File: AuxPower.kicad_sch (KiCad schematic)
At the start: 10 parts, among them J1 Conn_01x02_Female, U1 I6A4W020A033V-003-R

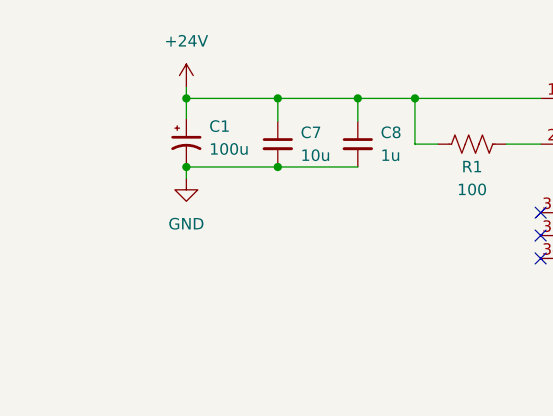
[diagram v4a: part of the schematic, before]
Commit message: Added 5V 9A buck converter
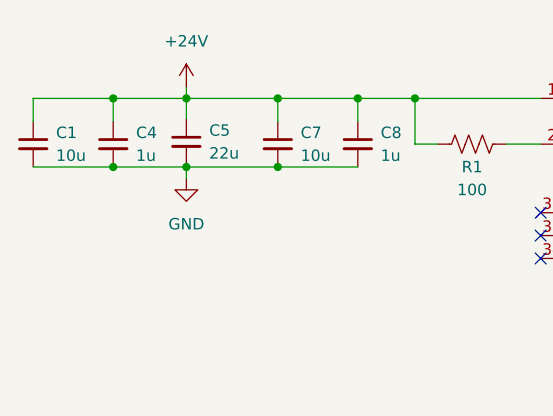
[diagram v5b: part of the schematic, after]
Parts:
- removed C1: 100u, Capacitor_SMD:CP_Elec_10x10, symbol Device:C_Polarized_Small_US
- added C1: 10u, Capacitor_SMD:C_0603_1608Metric, symbol Device:C_Small
- added C4: 1u, Capacitor_SMD:C_0603_1608Metric, symbol Device:C_Small
- added C5: 22u, Capacitor_Tantalum_SMD:CP_EIA-7343-15_Kemet-W, symbol Device:C_Small
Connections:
- net +24V: now also C1.1, C4.1, C5.1
- net GND: now also C1.2, C4.2, C5.2
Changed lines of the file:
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@@
 (kicad_sch (version 20211123) (generator eeschema)
   (paper "A4")
+  (junction (at 97.536 94.234) (diameter 0) (color 0 0 0 0)
+  )
+  (junction (at 79.248 94.234) (diameter 0) (color 0 0 0 0)
+  )
   (junction (at 157.226 86.614) (diameter 0) (color 0 0 0 0)
   )
@@
   (junction (at 171.196 94.234) (diameter 0) (color 0 0 0 0)
   )
-  (junction (at 97.536 94.234) (diameter 0) (color 0 0 0 0)
-  )
   (junction (at 87.376 86.614) (diameter 0) (color 0 0 0 0)
   )
   (junction (at 171.196 86.614) (diameter 0) (color 0 0 0 0)
   )
+  (junction (at 79.248 86.614) (diameter 0) (color 0 0 0 0)
+  )
   (junction (at 97.536 86.614) (diameter 0) (color 0 0 0 0)
   )
   (junction (at 149.606 112.014) (diameter 0) (color 0 0 0 0)
   )
+  (junction (at 87.376 94.234) (diameter 0) (color 0 0 0 0)
+  )
   (junction (at 141.986 112.014) (diameter 0) (color 0 0 0 0)
   )
@@
   )
   (junction (at 112.776 86.614) (diameter 0) (color 0 0 0 0)
-  )
-  (junction (at 87.376 94.234) (diameter 0) (color 0 0 0 0)
   )
   (junction (at 106.426 86.614) (diameter 0) (color 0 0 0 0)
@@
     (stroke (width 0) (type default) (color 0 0 0 0))
   )
+  (wire (pts (xy 70.358 94.234) (xy 79.248 94.234))
+    (stroke (width 0) (type default) (color 0 0 0 0))
+  )
   (wire (pts (xy 182.626 94.234) (xy 171.196 94.234))
     (stroke (width 0) (type default) (color 0 0 0 0))
@@
     (stroke (width 0) (type default) (color 0 0 0 0))
   )
-  (wire (pts (xy 87.376 94.234) (xy 97.536 94.234))
-    (stroke (width 0) (type default) (color 0 0 0 0))
-  )
   (wire (pts (xy 97.536 86.614) (xy 106.426 86.614))
     (stroke (width 0) (type default) (color 0 0 0 0))
@@
     (stroke (width 0) (type default) (color 0 0 0 0))
   )
+  (wire (pts (xy 70.358 86.614) (xy 79.248 86.614))
+    (stroke (width 0) (type default) (color 0 0 0 0))
+  )
   (wire (pts (xy 115.316 91.694) (xy 112.776 91.694))
     (stroke (width 0) (type default) (color 0 0 0 0))
   )
+  (wire (pts (xy 175.006 86.614) (xy 182.626 86.614))
+    (stroke (width 0) (type default) (color 0 0 0 0))
+  )
+  (wire (pts (xy 70.358 89.154) (xy 70.358 86.614))
+    (stroke (width 0) (type default) (color 0 0 0 0))
+  )
+  (wire (pts (xy 79.248 86.614) (xy 87.376 86.614))
+    (stroke (width 0) (type default) (color 0 0 0 0))
+  )
+  (wire (pts (xy 152.146 112.014) (xy 152.146 115.824))
+    (stroke (width 0) (type default) (color 0 0 0 0))
+  )
+  (wire (pts (xy 97.536 94.234) (xy 87.376 94.234))
+    (stroke (width 0) (type default) (color 0 0 0 0))
+  )
+  (wire (pts (xy 87.376 85.344) (xy 87.376 86.614))
+    (stroke (width 0) (type default) (color 0 0 0 0))
+  )
+  (wire (pts (xy 141.986 112.014) (xy 149.606 112.014))
+    (stroke (width 0) (type default) (color 0 0 0 0))
+  )
+  (wire (pts (xy 171.196 94.234) (xy 171.196 92.964))
+    (stroke (width 0) (type default) (color 0 0 0 0))
+  )
+  (wire (pts (xy 79.248 86.614) (xy 79.248 89.154))
+    (stroke (width 0) (type default) (color 0 0 0 0))
+  )
+  (wire (pts (xy 97.536 94.234) (xy 106.426 94.234))
+    (stroke (width 0) (type default) (color 0 0 0 0))
+  )
+  (wire (pts (xy 141.986 112.014) (xy 141.986 114.554))
+    (stroke (width 0) (type default) (color 0 0 0 0))
+  )
+  (wire (pts (xy 134.366 112.014) (xy 141.986 112.014))
+    (stroke (width 0) (type default) (color 0 0 0 0))
+  )
+  (wire (pts (xy 162.306 109.474) (xy 162.306 112.014))
+    (stroke (width 0) (type default) (color 0 0 0 0))
+  )
+  (wire (pts (xy 162.306 94.234) (xy 162.306 92.964))
+    (stroke (width 0) (type default) (color 0 0 0 0))
+  )
+  (wire (pts (xy 171.196 86.614) (xy 171.196 87.884))
+    (stroke (width 0) (type default) (color 0 0 0 0))
+  )
+  (wire (pts (xy 79.248 94.234) (xy 87.376 94.234))
+    (stroke (width 0) (type default) (color 0 0 0 0))
+  )
+  (wire (pts (xy 106.426 86.614) (xy 106.426 89.154))
+    (stroke (width 0) (type default) (color 0 0 0 0))
+  )
+  (wire (pts (xy 152.146 115.824) (xy 158.496 115.824))
+    (stroke (width 0) (type default) (color 0 0 0 0))
+  )
   (wire (pts (xy 87.376 94.234) (xy 87.376 95.504))
     (stroke (width 0) (type default) (color 0 0 0 0))
   )
-  (wire (pts (xy 175.006 86.614) (xy 182.626 86.614))
-    (stroke (width 0) (type default) (color 0 0 0 0))
-  )
-  (wire (pts (xy 152.146 112.014) (xy 152.146 115.824))
-    (stroke (width 0) (type default) (color 0 0 0 0))
-  )
-  (wire (pts (xy 87.376 85.344) (xy 87.376 86.614))
-    (stroke (width 0) (type default) (color 0 0 0 0))
-  )
-  (wire (pts (xy 141.986 112.014) (xy 149.606 112.014))
-    (stroke (width 0) (type default) (color 0 0 0 0))
-  )
-  (wire (pts (xy 171.196 94.234) (xy 171.196 92.964))
-    (stroke (width 0) (type default) (color 0 0 0 0))
-  )
-  (wire (pts (xy 97.536 94.234) (xy 106.426 94.234))
-    (stroke (width 0) (type default) (color 0 0 0 0))
-  )
-  (wire (pts (xy 141.986 112.014) (xy 141.986 114.554))
-    (stroke (width 0) (type default) (color 0 0 0 0))
-  )
-  (wire (pts (xy 134.366 112.014) (xy 141.986 112.014))
-    (stroke (width 0) (type default) (color 0 0 0 0))
-  )
-  (wire (pts (xy 162.306 109.474) (xy 162.306 112.014))
-    (stroke (width 0) (type default) (color 0 0 0 0))
-  )
-  (wire (pts (xy 162.306 94.234) (xy 162.306 92.964))
-    (stroke (width 0) (type default) (color 0 0 0 0))
-  )
-  (wire (pts (xy 171.196 86.614) (xy 171.196 87.884))
-    (stroke (width 0) (type default) (color 0 0 0 0))
-  )
-  (wire (pts (xy 106.426 86.614) (xy 106.426 89.154))
-    (stroke (width 0) (type default) (color 0 0 0 0))
-  )
-  (wire (pts (xy 152.146 115.824) (xy 158.496 115.824))
-    (stroke (width 0) (type default) (color 0 0 0 0))
-  )
   (wire (pts (xy 171.196 86.614) (xy 175.006 86.614))
     (stroke (width 0) (type default) (color 0 0 0 0))
@@
   (wire (pts (xy 157.226 86.614) (xy 162.306 86.614))
     (stroke (width 0) (type default) (color 0 0 0 0))
+  )
+  (symbol (lib_id "Device:C_Small") (at 79.248 91.694 0) (unit 1)
+    (in_bom yes) (on_board yes) (fields_autoplaced)
+    (property "Reference" "C4" (id 0) (at 81.788 90.4302 0)
+      (effects (font (size 1.27 1.27)) (justify left))
+    )
+    (property "Value" "1u" (id 1) (at 81.788 92.9702 0)
+      (effects (font (size 1.27 1.27)) (justify left))
+    )
+    (property "Footprint" "Capacitor_SMD:C_0603_1608Metric" (id 2) (at 79.248 91.694 0)
+      (effects (font (size 1.27 1.27)) hide)
+    )
+    (property "Datasheet" "~" (id 3) (at 79.248 91.694 0)
+      (effects (font (size 1.27 1.27)) hide)
+    )
+    (pin "1")
+    (pin "2")
   )
   (symbol (lib_id "power:+24V") (at 87.376 85.344 0) (unit 1)
@@
     (pin "2")
   )
+  (symbol (lib_id "Device:C_Small") (at 70.358 91.694 0) (unit 1)
+    (in_bom yes) (on_board yes) (fields_autoplaced)
+    (property "Reference" "C1" (id 0) (at 72.898 90.4302 0)
+      (effects (font (size 1.27 1.27)) (justify left))
+    )
+    (property "Value" "10u" (id 1) (at 72.898 92.9702 0)
+      (effects (font (size 1.27 1.27)) (justify left))
+    )
+    (property "Footprint" "Capacitor_SMD:C_0603_1608Metric" (id 2) (at 70.358 91.694 0)
+      (effects (font (size 1.27 1.27)) hide)
+    )
+    (property "Datasheet" "~" (id 3) (at 70.358 91.694 0)
+      (effects (font (size 1.27 1.27)) hide)
+    )
+    (pin "1")
+    (pin "2")
+  )
   (symbol (lib_id "Device:C_Small") (at 106.426 91.694 0) (unit 1)
     (in_bom yes) (on_board yes) (fields_autoplaced)
@@
     )
     (pin "1")
+  )
+  (symbol (lib_id "Device:C_Small") (at 87.376 91.44 0) (unit 1)
+    (in_bom yes) (on_board yes) (fields_autoplaced)
+    (property "Reference" "C5" (id 0) (at 89.916 90.1762 0)
+      (effects (font (size 1.27 1.27)) (justify left))
+    )
+    (property "Value" "22u" (id 1) (at 89.916 92.7162 0)
+      (effects (font (size 1.27 1.27)) (justify left))
+    )
+    (property "Footprint" "Capacitor_Tantalum_SMD:CP_EIA-7343-15_Kemet-W" (id 2) (at 87.376 91.44 0)
+      (effects (font (size 1.27 1.27)) hide)
+    )
+    (property "Datasheet" "~" (id 3) (at 87.376 91.44 0)
+      (effects (font (size 1.27 1.27)) hide)
+    )
+    (pin "1")
+    (pin "2")
   )
   (symbol (lib_id "Device:R_US") (at 119.126 91.694 90) (unit 1)
@@
     (pin "1")
   )
-  (symbol (lib_id "Device:C_Polarized_Small_US") (at 87.376 91.44 0) (unit 1)
-    (in_bom yes) (on_board yes) (fields_autoplaced)
-    (property "Reference" "C1" (id 0) (at 89.916 89.7381 0)
-      (effects (font (size 1.27 1.27)) (justify left))
-    )
-    (property "Value" "100u" (id 1) (at 89.916 92.2781 0)
-      (effects (font (size 1.27 1.27)) (justify left))
-    )
-    (property "Footprint" "Capacitor_SMD:CP_Elec_10x10" (id 2) (at 87.376 91.44 0)
-      (effects (font (size 1.27 1.27)) hide)
-    )
-    (property "Datasheet" "~" (id 3) (at 87.376 91.44 0)
-      (effects (font (size 1.27 1.27)) hide)
-    )
-    (pin "1")
-    (pin "2")
-  )
 )

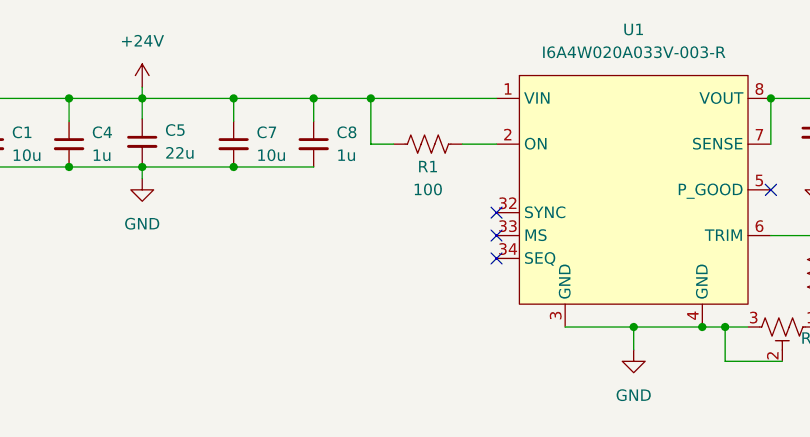
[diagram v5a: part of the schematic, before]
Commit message: fixed 9V regulator circuit
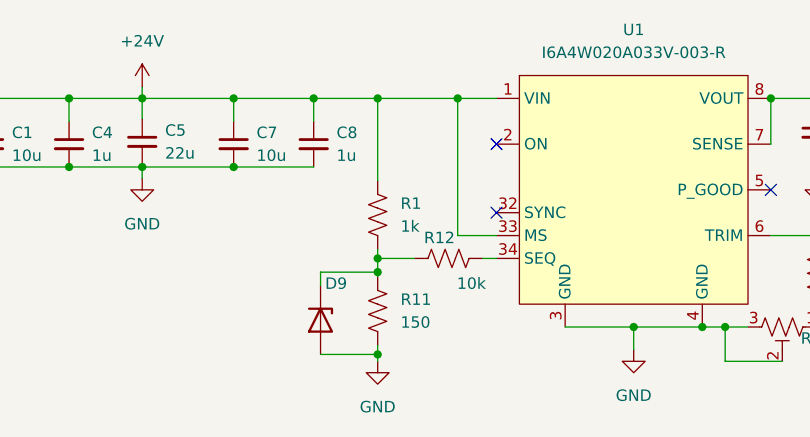
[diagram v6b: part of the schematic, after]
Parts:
- added D9: BZX8450-C2V2VL, Package_TO_SOT_SMD:SOT-23, symbol Device:D_Zener
- added R11: 150, Resistor_SMD:R_0805_2012Metric, symbol Device:R_US
- added R12: 10k, Resistor_SMD:R_0805_2012Metric, symbol Device:R_US
- R1: value 100 -> 1k
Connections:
- net +24V: now also U1.33 (MS)
- net GND: now also D9.1 (A), R11.2
- net at R1.2: now also D9.3 (K), R11.1, R12.1; no longer U1.2 (ON)
- net at U1.34 (SEQ): now also R12.2
- no-connect marks 4 -> 3
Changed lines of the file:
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@@
 (kicad_sch (version 20211123) (generator eeschema)
   (paper "A4")
+  (junction (at 113.538 86.614) (diameter 0) (color 0 0 0 0)
+  )
   (junction (at 97.536 94.234) (diameter 0) (color 0 0 0 0)
   )
@@
   (junction (at 152.146 112.014) (diameter 0) (color 0 0 0 0)
   )
+  (junction (at 113.538 105.918) (diameter 0) (color 0 0 0 0)
+  )
+  (junction (at 122.428 86.614) (diameter 0) (color 0 0 0 0)
+  )
+  (junction (at 113.538 104.394) (diameter 0) (color 0 0 0 0)
+  )
   (junction (at 162.306 94.234) (diameter 0) (color 0 0 0 0)
   )
@@
   (junction (at 97.536 86.614) (diameter 0) (color 0 0 0 0)
   )
+  (junction (at 113.538 115.062) (diameter 0) (color 0 0 0 0)
+  )
   (junction (at 149.606 112.014) (diameter 0) (color 0 0 0 0)
   )
@@
   (junction (at 162.306 86.614) (diameter 0) (color 0 0 0 0)
   )
-  (junction (at 112.776 86.614) (diameter 0) (color 0 0 0 0)
-  )
   (junction (at 106.426 86.614) (diameter 0) (color 0 0 0 0)
   )
   (no_connect (at 157.226 96.774))
+  (no_connect (at 126.746 91.694))
   (no_connect (at 126.746 99.314))
-  (no_connect (at 126.746 104.394))
-  (no_connect (at 126.746 101.854))
   (wire (pts (xy 97.536 89.154) (xy 97.536 86.614))
     (stroke (width 0) (type default) (color 0 0 0 0))
   )
+  (wire (pts (xy 117.602 104.394) (xy 113.538 104.394))
+    (stroke (width 0) (type default) (color 0 0 0 0))
+  )
   (wire (pts (xy 157.226 86.614) (xy 157.226 91.694))
     (stroke (width 0) (type default) (color 0 0 0 0))
@@
     (stroke (width 0) (type default) (color 0 0 0 0))
   )
+  (wire (pts (xy 107.188 115.062) (xy 113.538 115.062))
+    (stroke (width 0) (type default) (color 0 0 0 0))
+  )
+  (wire (pts (xy 126.746 104.394) (xy 125.222 104.394))
+    (stroke (width 0) (type default) (color 0 0 0 0))
+  )
   (wire (pts (xy 87.376 93.98) (xy 87.376 94.234))
     (stroke (width 0) (type default) (color 0 0 0 0))
@@
     (stroke (width 0) (type default) (color 0 0 0 0))
   )
+  (wire (pts (xy 113.538 115.062) (xy 113.538 115.824))
+    (stroke (width 0) (type default) (color 0 0 0 0))
+  )
   (wire (pts (xy 157.226 101.854) (xy 162.306 101.854))
     (stroke (width 0) (type default) (color 0 0 0 0))
   )
-  (wire (pts (xy 106.426 86.614) (xy 112.776 86.614))
-    (stroke (width 0) (type default) (color 0 0 0 0))
-  )
   (wire (pts (xy 70.358 94.234) (xy 79.248 94.234))
     (stroke (width 0) (type default) (color 0 0 0 0))
@@
     (stroke (width 0) (type default) (color 0 0 0 0))
   )
-  (wire (pts (xy 126.746 91.694) (xy 122.936 91.694))
-    (stroke (width 0) (type default) (color 0 0 0 0))
-  )
-  (wire (pts (xy 112.776 86.614) (xy 126.746 86.614))
+  (wire (pts (xy 106.426 86.614) (xy 113.538 86.614))
     (stroke (width 0) (type default) (color 0 0 0 0))
   )
@@
     (stroke (width 0) (type default) (color 0 0 0 0))
   )
-  (wire (pts (xy 112.776 91.694) (xy 112.776 86.614))
-    (stroke (width 0) (type default) (color 0 0 0 0))
-  )
   (wire (pts (xy 70.358 86.614) (xy 79.248 86.614))
     (stroke (width 0) (type default) (color 0 0 0 0))
   )
-  (wire (pts (xy 115.316 91.694) (xy 112.776 91.694))
+  (wire (pts (xy 113.538 103.378) (xy 113.538 104.394))
     (stroke (width 0) (type default) (color 0 0 0 0))
   )
@@
     (stroke (width 0) (type default) (color 0 0 0 0))
   )
+  (wire (pts (xy 122.428 101.854) (xy 122.428 86.614))
+    (stroke (width 0) (type default) (color 0 0 0 0))
+  )
+  (wire (pts (xy 113.538 95.758) (xy 113.538 86.614))
+    (stroke (width 0) (type default) (color 0 0 0 0))
+  )
+  (wire (pts (xy 107.188 107.442) (xy 107.188 105.918))
+    (stroke (width 0) (type default) (color 0 0 0 0))
+  )
   (wire (pts (xy 70.358 89.154) (xy 70.358 86.614))
     (stroke (width 0) (type default) (color 0 0 0 0))
@@
     (stroke (width 0) (type default) (color 0 0 0 0))
   )
+  (wire (pts (xy 122.428 86.614) (xy 126.746 86.614))
+    (stroke (width 0) (type default) (color 0 0 0 0))
+  )
   (wire (pts (xy 152.146 112.014) (xy 152.146 115.824))
     (stroke (width 0) (type default) (color 0 0 0 0))
   )
+  (wire (pts (xy 126.746 101.854) (xy 122.428 101.854))
+    (stroke (width 0) (type default) (color 0 0 0 0))
+  )
   (wire (pts (xy 97.536 94.234) (xy 87.376 94.234))
     (stroke (width 0) (type default) (color 0 0 0 0))
@@
     (stroke (width 0) (type default) (color 0 0 0 0))
   )
+  (wire (pts (xy 113.538 104.394) (xy 113.538 105.918))
+    (stroke (width 0) (type default) (color 0 0 0 0))
+  )
+  (wire (pts (xy 113.538 105.918) (xy 113.538 106.426))
+    (stroke (width 0) (type default) (color 0 0 0 0))
+  )
   (wire (pts (xy 171.196 94.234) (xy 171.196 92.964))
     (stroke (width 0) (type default) (color 0 0 0 0))
@@
     (stroke (width 0) (type default) (color 0 0 0 0))
   )
+  (wire (pts (xy 107.188 105.918) (xy 113.538 105.918))
+    (stroke (width 0) (type default) (color 0 0 0 0))
+  )
   (wire (pts (xy 97.536 94.234) (xy 106.426 94.234))
     (stroke (width 0) (type default) (color 0 0 0 0))
   )
+  (wire (pts (xy 113.538 115.062) (xy 113.538 114.046))
+    (stroke (width 0) (type default) (color 0 0 0 0))
+  )
   (wire (pts (xy 141.986 112.014) (xy 141.986 114.554))
+    (stroke (width 0) (type default) (color 0 0 0 0))
+  )
+  (wire (pts (xy 113.538 86.614) (xy 122.428 86.614))
     (stroke (width 0) (type default) (color 0 0 0 0))
   )
@@
     (pin "2")
   )
+  (symbol (lib_id "Device:R_US") (at 121.412 104.394 90) (unit 1)
+    (in_bom yes) (on_board yes)
+    (property "Reference" "R12" (id 0) (at 120.396 102.108 90))
+    (property "Value" "10k" (id 1) (at 123.952 107.188 90))
+    (property "Footprint" "Resistor_SMD:R_0805_2012Metric" (id 2) (at 121.666 103.378 90)
+      (effects (font (size 1.27 1.27)) hide)
+    )
+    (property "Datasheet" "~" (id 3) (at 121.412 104.394 0)
+      (effects (font (size 1.27 1.27)) hide)
+    )
+    (pin "1")
+    (pin "2")
+  )
   (symbol (lib_id "Device:C_Small") (at 171.196 90.424 0) (unit 1)
     (in_bom yes) (on_board yes) (fields_autoplaced)
@@
     (pin "2")
   )
-  (symbol (lib_id "Device:R_US") (at 119.126 91.694 90) (unit 1)
-    (in_bom yes) (on_board yes)
-    (property "Reference" "R1" (id 0) (at 119.126 94.234 90))
-    (property "Value" "100" (id 1) (at 119.126 96.774 90))
-    (property "Footprint" "Resistor_SMD:R_0805_2012Metric" (id 2) (at 119.38 90.678 90)
-      (effects (font (size 1.27 1.27)) hide)
-    )
-    (property "Datasheet" "~" (id 3) (at 119.126 91.694 0)
+  (symbol (lib_id "power:GND") (at 113.538 115.824 0) (unit 1)
+    (in_bom yes) (on_board yes) (fields_autoplaced)
+    (property "Reference" "#PWR0118" (id 0) (at 113.538 122.174 0)
+      (effects (font (size 1.27 1.27)) hide)
+    )
+    (property "Value" "GND" (id 1) (at 113.538 120.904 0))
+    (property "Footprint" "" (id 2) (at 113.538 115.824 0)
+      (effects (font (size 1.27 1.27)) hide)
+    )
+    (property "Datasheet" "" (id 3) (at 113.538 115.824 0)
+      (effects (font (size 1.27 1.27)) hide)
+    )
+    (pin "1")
+  )
+  (symbol (lib_id "Device:R_US") (at 113.538 110.236 0) (unit 1)
+    (in_bom yes) (on_board yes) (fields_autoplaced)
+    (property "Reference" "R11" (id 0) (at 116.078 108.9659 0)
+      (effects (font (size 1.27 1.27)) (justify left))
+    )
+    (property "Value" "150" (id 1) (at 116.078 111.5059 0)
+      (effects (font (size 1.27 1.27)) (justify left))
+    )
+    (property "Footprint" "Resistor_SMD:R_0805_2012Metric" (id 2) (at 114.554 110.49 90)
+      (effects (font (size 1.27 1.27)) hide)
+    )
+    (property "Datasheet" "~" (id 3) (at 113.538 110.236 0)
       (effects (font (size 1.27 1.27)) hide)
     )
@@
     (pin "2")
     (pin "3")
+  )
+  (symbol (lib_id "Device:D_Zener") (at 107.188 111.252 270) (unit 1)
+    (in_bom yes) (on_board yes)
+    (property "Reference" "D9" (id 0) (at 107.696 107.188 90)
+      (effects (font (size 1.27 1.27)) (justify left))
+    )
+    (property "Value" "BZX8450-C2V2VL" (id 1) (at 104.648 105.41 90)
+      (effects (font (size 1.27 1.27)) (justify left) hide)
+    )
+    (property "Footprint" "Package_TO_SOT_SMD:SOT-23" (id 2) (at 107.188 111.252 0)
+      (effects (font (size 1.27 1.27)) hide)
+    )
+    (property "Datasheet" "~" (id 3) (at 107.188 111.252 0)
+      (effects (font (size 1.27 1.27)) hide)
+    )
+    (property "MFN#" "BZX8450-C2V2VL" (id 4) (at 107.188 111.252 90)
+      (effects (font (size 1.27 1.27)) hide)
+    )
+    (pin "3")
+    (pin "1")
   )
   (symbol (lib_id "Device:C_Small") (at 162.306 90.424 0) (unit 1)
@@
     (pin "1")
   )
+  (symbol (lib_id "Device:R_US") (at 113.538 99.568 0) (unit 1)
+    (in_bom yes) (on_board yes) (fields_autoplaced)
+    (property "Reference" "R1" (id 0) (at 116.078 98.2979 0)
+      (effects (font (size 1.27 1.27)) (justify left))
+    )
+    (property "Value" "1k" (id 1) (at 116.078 100.8379 0)
+      (effects (font (size 1.27 1.27)) (justify left))
+    )
+    (property "Footprint" "Resistor_SMD:R_0805_2012Metric" (id 2) (at 114.554 99.822 90)
+      (effects (font (size 1.27 1.27)) hide)
+    )
+    (property "Datasheet" "~" (id 3) (at 113.538 99.568 0)
+      (effects (font (size 1.27 1.27)) hide)
+    )
+    (pin "1")
+    (pin "2")
+  )
 )
